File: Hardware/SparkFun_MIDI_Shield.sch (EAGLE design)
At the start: 36 parts, among them J1 MIDI IN, J2 MIDI OUT, J3 UNO_R3_SHIELD, U1 6N138M, U2 74AHC1G125

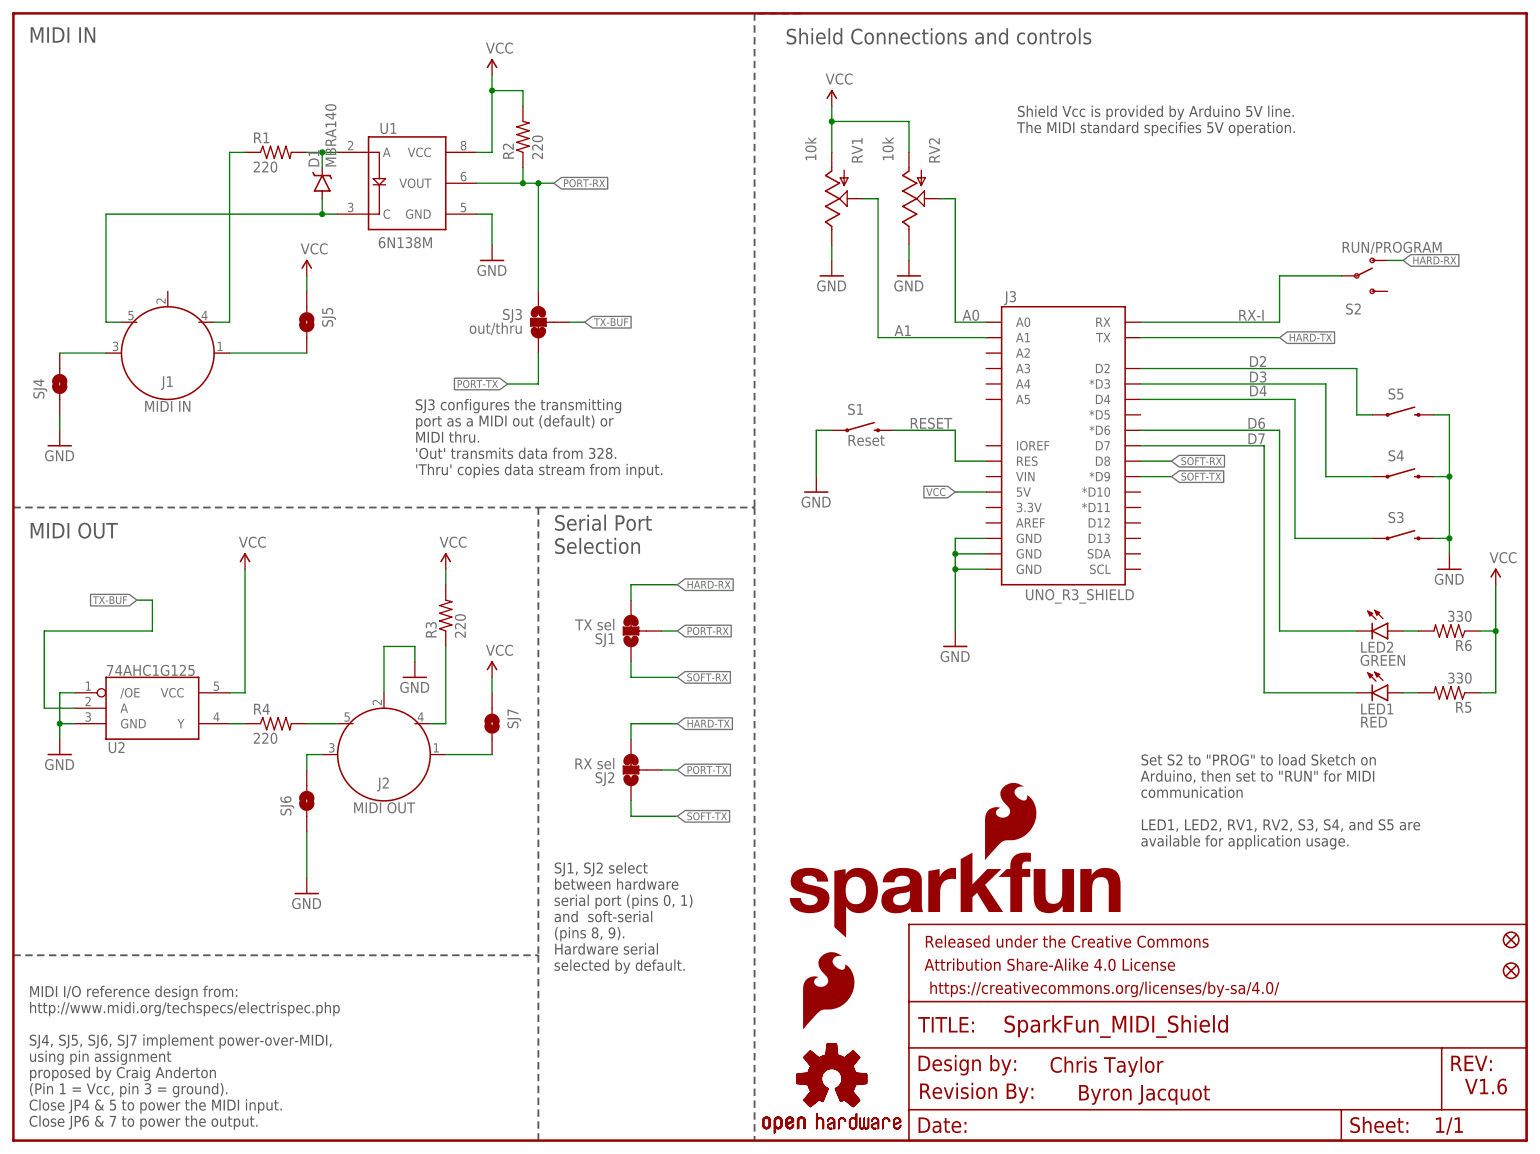
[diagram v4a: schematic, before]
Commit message: Updates based on QC checklist.
-Measures layer populated.
-U1 got name/value.
-Added stubs to some parts on schem.
-Version # back to 1.5.
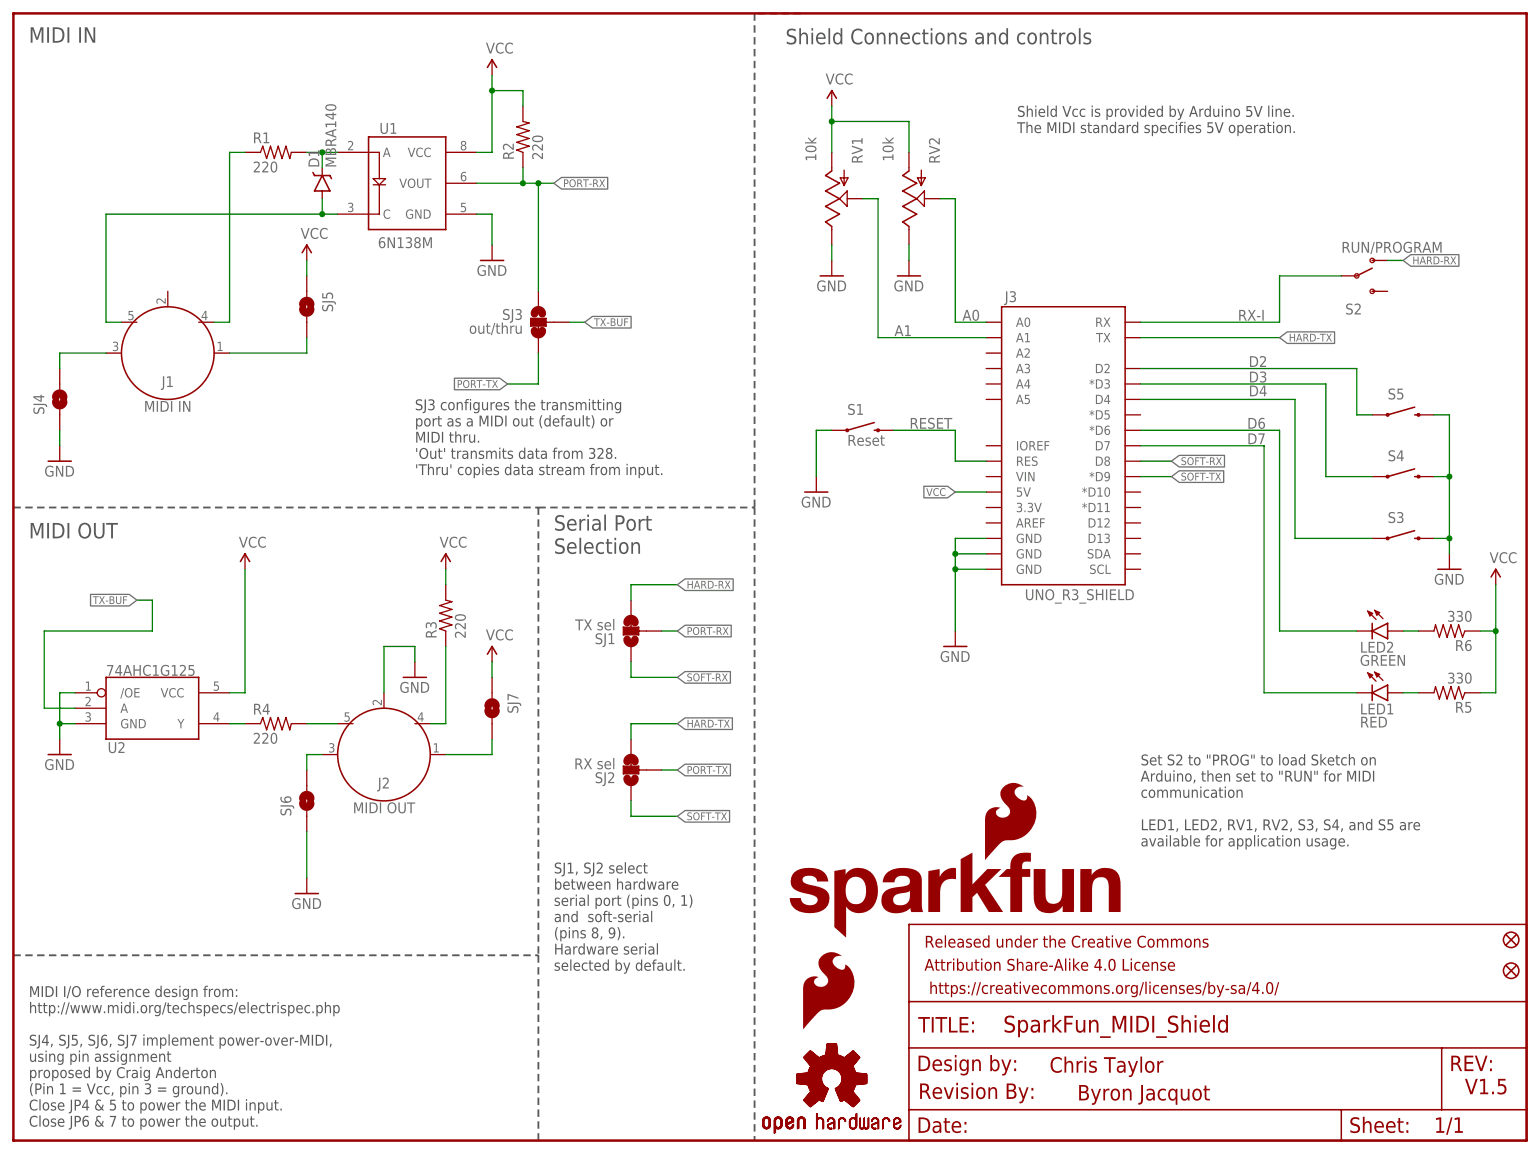
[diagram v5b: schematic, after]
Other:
- note added: "V1.5"
- note removed: "V1.6"
- moved on the sheet: SJ4, SJ5, SJ7
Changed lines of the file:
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@@
 <text x="2.54" y="99.06" size="2.54" layer="97">MIDI OUT</text>
 <text x="175.006" y="6.604" size="2.54" layer="94">Byron Jacquot</text>
-<text x="238.76" y="7.62" size="2.54" layer="94">V1.6</text>
+<text x="238.76" y="7.62" size="2.54" layer="94">V1.5</text>
 <wire x1="129.54" y1="185.42" x2="121.92" y2="185.42" width="0.3048" layer="94" style="shortdash"/>
 <wire x1="121.92" y1="185.42" x2="121.92" y2="104.14" width="0.3048" layer="97" style="shortdash"/>
@@
 <attribute name="NAME" x="45.72" y="53.34" size="1.778" layer="95" rot="R90"/>
 </instance>
-<instance part="SJ7" gate="G$1" x="78.74" y="68.58" smashed="yes" rot="R270">
-<attribute name="NAME" x="81.28" y="71.12" size="1.778" layer="95" rot="R270"/>
-</instance>
-<instance part="SJ4" gate="G$1" x="7.62" y="124.46" smashed="yes" rot="R90">
-<attribute name="NAME" x="5.08" y="121.92" size="1.778" layer="95" rot="R90"/>
-</instance>
-<instance part="SJ5" gate="G$1" x="48.26" y="134.62" smashed="yes" rot="R270">
-<attribute name="NAME" x="50.8" y="137.16" size="1.778" layer="95" rot="R270"/>
-</instance>
-<instance part="P+6" gate="1" x="78.74" y="76.2"/>
-<instance part="P+7" gate="1" x="48.26" y="142.24"/>
-<instance part="GND9" gate="1" x="7.62" y="114.3"/>
+<instance part="SJ7" gate="G$1" x="78.74" y="71.12" smashed="yes" rot="R270">
+<attribute name="NAME" x="81.28" y="73.66" size="1.778" layer="95" rot="R270"/>
+</instance>
+<instance part="SJ4" gate="G$1" x="7.62" y="121.92" smashed="yes" rot="R90">
+<attribute name="NAME" x="5.08" y="119.38" size="1.778" layer="95" rot="R90"/>
+</instance>
+<instance part="SJ5" gate="G$1" x="48.26" y="137.16" smashed="yes" rot="R270">
+<attribute name="NAME" x="50.8" y="139.7" size="1.778" layer="95" rot="R270"/>
+</instance>
+<instance part="P+6" gate="1" x="78.74" y="78.74"/>
+<instance part="P+7" gate="1" x="48.26" y="144.78"/>
+<instance part="GND9" gate="1" x="7.62" y="111.76"/>
 <instance part="GND10" gate="1" x="48.26" y="40.64"/>
 <instance part="LOGO1" gate="G$1" x="127" y="33.02"/>
@@
 <pinref part="SJ4" gate="G$1" pin="1"/>
 <pinref part="GND9" gate="1" pin="GND"/>
-<wire x1="7.62" y1="119.38" x2="7.62" y2="116.84" width="0.1524" layer="91"/>
+<wire x1="7.62" y1="116.84" x2="7.62" y2="114.3" width="0.1524" layer="91"/>
 </segment>
 <segment>
@@
 <segment>
 <pinref part="SJ7" gate="G$1" pin="1"/>
-<wire x1="78.74" y1="73.66" x2="78.74" y2="76.2" width="0.1524" layer="91"/>
+<wire x1="78.74" y1="76.2" x2="78.74" y2="78.74" width="0.1524" layer="91"/>
 <pinref part="P+6" gate="1" pin="VCC"/>
 </segment>
@@
 <pinref part="SJ5" gate="G$1" pin="1"/>
 <pinref part="P+7" gate="1" pin="VCC"/>
-<wire x1="48.26" y1="139.7" x2="48.26" y2="142.24" width="0.1524" layer="91"/>
+<wire x1="48.26" y1="142.24" x2="48.26" y2="144.78" width="0.1524" layer="91"/>
 </segment>
 </net>
@@
 <pinref part="J2" gate="G$1" pin="1"/>
 <wire x1="71.12" y1="63.5" x2="78.74" y2="63.5" width="0.1524" layer="91"/>
+<wire x1="78.74" y1="63.5" x2="78.74" y2="66.04" width="0.1524" layer="91"/>
 <pinref part="SJ7" gate="G$1" pin="2"/>
 </segment>
@@
 <segment>
 <pinref part="J1" gate="G$1" pin="3"/>
+<wire x1="7.62" y1="127" x2="7.62" y2="129.54" width="0.1524" layer="91"/>
 <wire x1="7.62" y1="129.54" x2="15.24" y2="129.54" width="0.1524" layer="91"/>
 <pinref part="SJ4" gate="G$1" pin="2"/>
@@
 <pinref part="J1" gate="G$1" pin="1"/>
 <wire x1="35.56" y1="129.54" x2="48.26" y2="129.54" width="0.1524" layer="91"/>
+<wire x1="48.26" y1="129.54" x2="48.26" y2="132.08" width="0.1524" layer="91"/>
 <pinref part="SJ5" gate="G$1" pin="2"/>
 </segment>

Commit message: Fixing QC review issue with LP1,2 naming.
TX & RX were transposed in jumper names.
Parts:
- SJ1: value TX sel -> RX sel
- SJ2: value RX sel -> TX sel
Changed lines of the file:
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@@
 <?xml version="1.0" encoding="utf-8"?>
 <!DOCTYPE eagle SYSTEM "eagle.dtd">
-<eagle version="7.1.0">
+<eagle version="7.3.0">
 <drawing>
 <settings>
@@
 <part name="LOGO3" library="SparkFun-Aesthetics" deviceset="OSHW-LOGO" device="M"/>
 <part name="LOGO5" library="SparkFun-Aesthetics" deviceset="SFE_LOGO_FLAME" device=".1_INCH"/>
-<part name="SJ1" library="SparkFun-Passives" deviceset="JUMPER-PAD-3-2OF3_NC_BY_TRACE" device="_SMALL" value="TX sel"/>
-<part name="SJ2" library="SparkFun-Passives" deviceset="JUMPER-PAD-3-2OF3_NC_BY_TRACE" device="_SMALL" value="RX sel"/>
+<part name="SJ1" library="SparkFun-Passives" deviceset="JUMPER-PAD-3-2OF3_NC_BY_TRACE" device="_SMALL" value="RX sel"/>
+<part name="SJ2" library="SparkFun-Passives" deviceset="JUMPER-PAD-3-2OF3_NC_BY_TRACE" device="_SMALL" value="TX sel"/>
 <part name="U1" library="SparkFun-DiscreteSemi" deviceset="OPTO_DARL_6N138S" device="" value="6N138M"/>
 <part name="SJ3" library="SparkFun-Passives" deviceset="JUMPER-PAD-3-2OF3_NC_BY_TRACE" device="_SMALL" value="out/thru"/>
